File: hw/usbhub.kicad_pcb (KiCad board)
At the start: 2 copper layers, 100 x 100 mm, 92 parts, among them J1 EXT_PWR, J2 USB_C_Receptacle_USB2.0, J3 USB6, J4 USB2, J5 USB7, J6 USB3, J7 USB4, J8 USB5, J9 SWD, SW1 SW_Push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

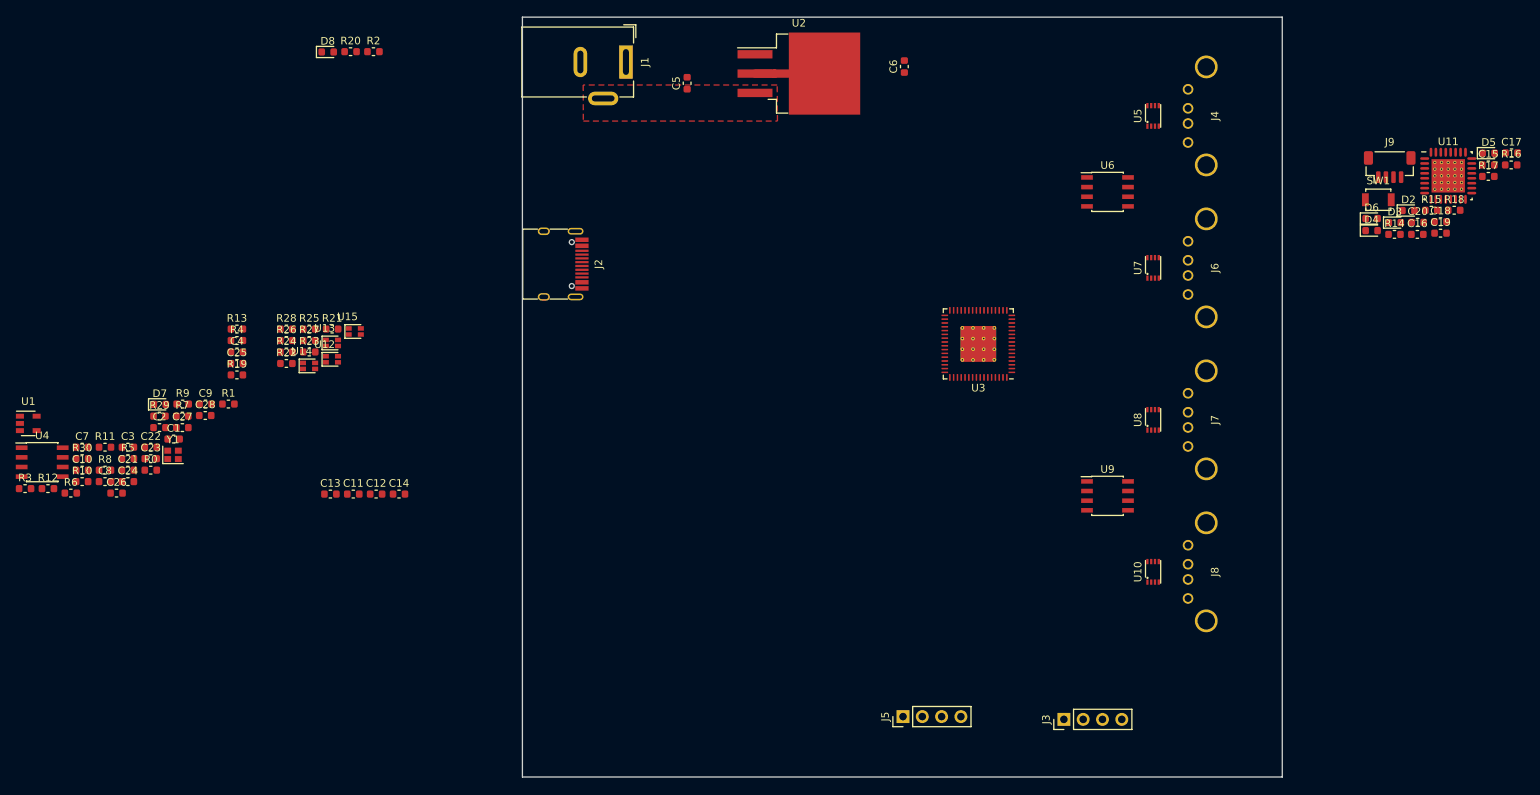
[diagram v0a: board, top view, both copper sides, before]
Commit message: More parts placement
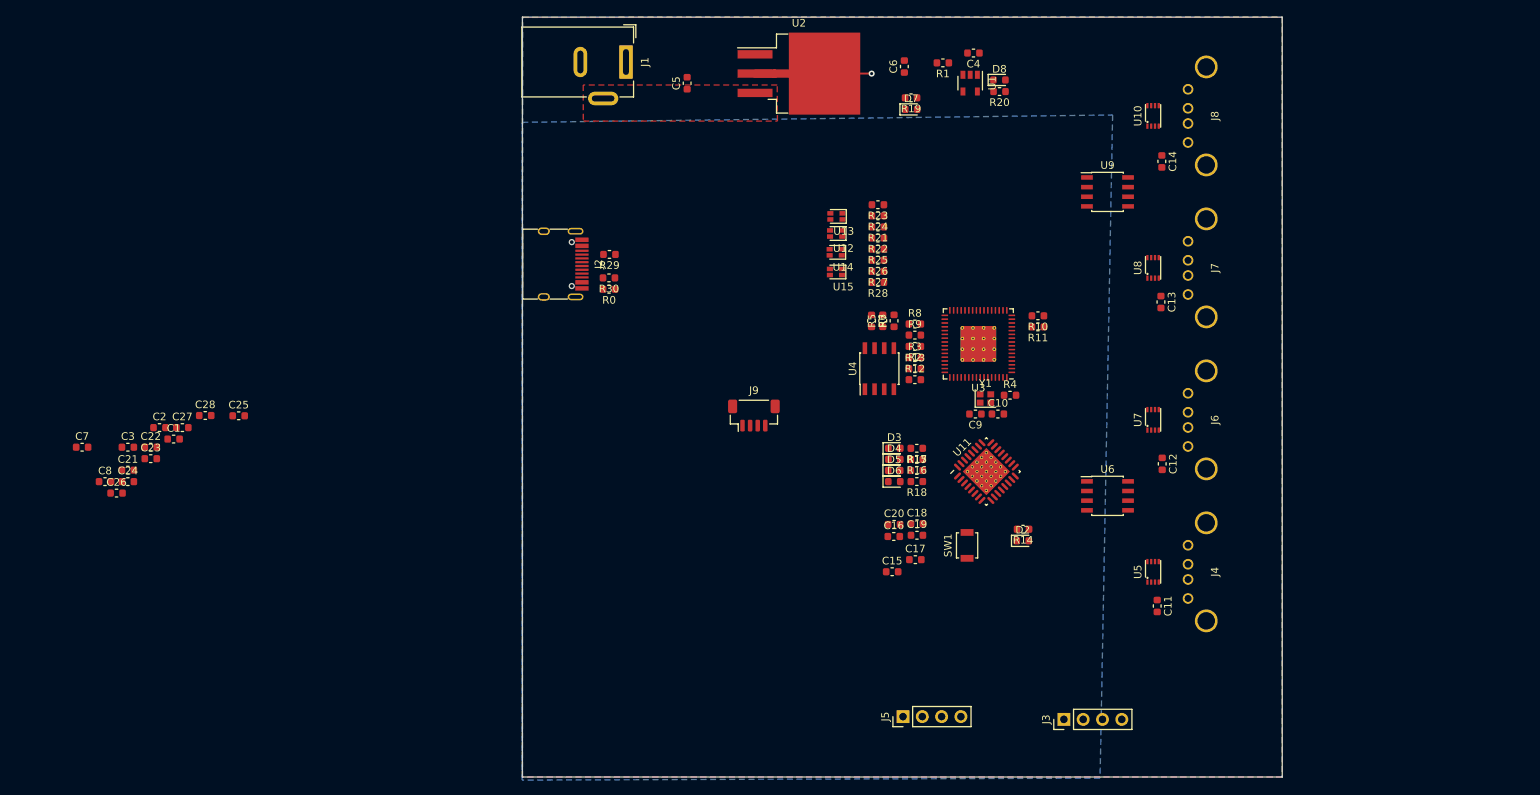
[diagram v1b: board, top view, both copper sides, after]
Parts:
- moved U1 131.8 mm to (158.9, 58.7), turned to 270 degrees
- moved R10 127.7 mm to (167.8, 89.3), turned to 180 degrees
- moved R11 123.8 mm to (167.8, 90.8), turned to 180 degrees
- moved C10 120.7 mm to (162.6, 102.2)
- moved R3 118.4 mm to (151.7, 94.8)
- moved R12 115.0 mm to (151.7, 97.7)
- moved C13 112.2 mm to (184.0, 87.5), turned to 270 degrees
- moved U4 110.9 mm to (147.0, 96.3), turned to 90 degrees
- moved C14 109.5 mm to (184.2, 69.0), turned to 270 degrees
- moved R8 108.3 mm to (151.7, 90.4)
- moved R6 107.8 mm to (145.9, 90.0), turned to 270 degrees
- moved Y1 107.2 mm to (160.9, 100.2)
- moved C11 106.8 mm to (183.5, 127.5), turned to 270 degrees
- moved D7 106.2 mm to (151.2, 62.1)
- moved C4 104.6 mm to (159.4, 54.7), turned to 180 degrees
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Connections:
- U6 pad 5: /USBPorts/USB3_VBUS -> /USBPorts/USB2_VBUS
- U6 pad 8: /USBPorts/USB2_VBUS -> /USBPorts/USB3_VBUS
- U9 pad 5: /USBPorts/USB5_VBUS -> /USBPorts/USB4_VBUS
- U9 pad 8: /USBPorts/USB4_VBUS -> /USBPorts/USB5_VBUS
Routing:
- net +5V: track 9.15 -> 15.4 mm, vias 0 -> 1
- added copper zone on B.Cu, net +5V
- added copper zone on B.Cu, net GND
- added copper zone on F.Cu, net GND

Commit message: More placement, more issues
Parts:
- removed D6: LED_Small, LED_SMD:LED_0603_1608Metric
- removed R21, R22, R23, R24, R25, R26, R27, R28: 360R, Resistor_SMD:R_0603_1608Metric
- removed U12, U13, U14, U15: LED_GRAB, LED_SMD_Extra:LED_RGB_0606_1616Metric
- added D1: G, LED_SMD:LED_0603_1608Metric, F.Cu at (194.8, 107.7)
- C11, C12, C13, C14: footprint Capacitor_SMD:C_0603_1608Metric -> Capacitor_SMD:CP_Elec_5x5.8
- D2: value Green -> VDDMCU_LED
- D3, D4, D5: value LED_Small -> G
- R0: value 0R -> DNP
- R12: value 10k -> DNP
- R15: value 360R -> 2.2k
- R16, R17, R18: value R_Small -> 2.2k
- SW1: value SW_Push -> MCU_RESET
- moved D3 66.2 mm to (194.8, 59.0), turned to 180 degrees
- moved R16 62.6 mm to (190.5, 59.0), turned to 0 degrees
- moved D5 52.9 mm to (194.8, 83.2), turned to 180 degrees
- moved D4 52.2 mm to (194.8, 133.2), turned to 180 degrees
- moved R18 47.6 mm to (190.5, 83.2)
- moved R17 45.3 mm to (190.5, 133.3), turned to 180 degrees
- moved J5 42.6 mm to (107.7, 145.2)
- moved R15 38.7 mm to (190.5, 107.7), turned to 0 degrees
- moved C15 33.3 mm to (115.5, 119.8)
- moved C16 33.3 mm to (115.7, 115.2)
- moved D2 33.3 mm to (132.7, 115.8)
- moved R14 33.3 mm to (132.7, 114.2)
- moved C18 33.3 mm to (118.8, 113.5)
- moved C19 33.3 mm to (118.8, 115.0)
- moved C20 33.3 mm to (115.8, 113.6)
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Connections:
- net /USBPorts/USB_D+ renamed /USBPorts/USB3_D+
- net Net-(C10-Pad1) renamed /USB2517/XTAL1
- net Net-(C9-Pad1) renamed /USB2517/XTAL2
- net Net-(J2-PadA5) renamed /USB2517/CC1
- net Net-(J2-PadA6) renamed /USB2517/USBUP_D+
- net Net-(J2-PadA7) renamed /USB2517/USBUP_D-
- net Net-(J2-PadB5) renamed /USB2517/CC2
- net Net-(R1-Pad1) renamed /USB2517/3V3_EN
- net Net-(R10-Pad2) renamed /USB2517/CFG_SEL2
- net Net-(R2-Pad1) renamed /USB2517/VBUS_DET
- net Net-(R4-Pad1) renamed /USB2517/RBIAS
- net Net-(R8-Pad2) renamed /USB2517/CFG_SEL1
- net Net-(SW1-Pad2) renamed /MCU/~MCU_RESET~
- R15 pad 1: /MCU/PORT2_PWR -> /USBPorts/USB3_VBUS
- R15 pad 2: Net-(D3-Pad2) -> Net-(D1-Pad2)
- R16 pad 1: /MCU/PORT3_PWR -> /USBPorts/USB5_VBUS
- R16 pad 2: Net-(D4-Pad2) -> Net-(D3-Pad2)
- R17 pad 1: /MCU/PORT4_PWR -> Net-(D4-Pad2)
- R17 pad 2: Net-(D5-Pad2) -> /USBPorts/USB2_VBUS
- R18 pad 1: /MCU/PORT5_PWR -> Net-(D5-Pad2)
- R18 pad 2: Net-(D6-Pad2) -> /USBPorts/USB4_VBUS
- U3 pad 18: /USBPorts/PORT5_LED2 -> Net-(U3-Pad18)
- U3 pad 21: Net-(U3-Pad21) -> /USBPorts/USB4_OC
- U3 pad 22: Net-(U3-Pad22) -> /USBPorts/USB3_OC
- U3 pad 27: Net-(U3-Pad27) -> /USBPorts/USB2_OC
- U3 pad 31: /USBPorts/PORT5_LED1 -> Net-(U3-Pad31)
- U3 pad 32: /USBPorts/PORT4_LED2 -> Net-(U3-Pad32)
- U3 pad 33: /USBPorts/PORT4_LED1 -> Net-(U3-Pad33)
- U3 pad 34: /USBPorts/PORT3_LED2 -> Net-(U3-Pad34)
- U3 pad 35: Net-(U3-Pad35) -> /USBPorts/USB5_OC
- U3 pad 47: /USBPorts/PORT3_LED1 -> Net-(U3-Pad47)
- U3 pad 48: /USBPorts/PORT2_LED2 -> Net-(U3-Pad48)
- U3 pad 49: /USBPorts/PORT2_LED1 -> Net-(U3-Pad49)
- U6 pad 1: /MCU/PORT2_EN -> /MCU/PORT3_EN
- U6 pad 2: Net-(U3-Pad27) -> /USBPorts/USB3_OC
- U6 pad 3: Net-(U3-Pad22) -> /USBPorts/USB2_OC
- U6 pad 4: /MCU/PORT3_EN -> /MCU/PORT2_EN
- U9 pad 1: /MCU/PORT4_EN -> /MCU/PORT5_EN
- U9 pad 2: Net-(U3-Pad21) -> /USBPorts/USB5_OC
- U9 pad 3: Net-(U3-Pad35) -> /USBPorts/USB4_OC
- U9 pad 4: /MCU/PORT5_EN -> /MCU/PORT4_EN
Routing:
- net +5V: track 15.4 -> 13.5 mm, vias 1 -> 14
- added copper zone on F.Cu, net +5V

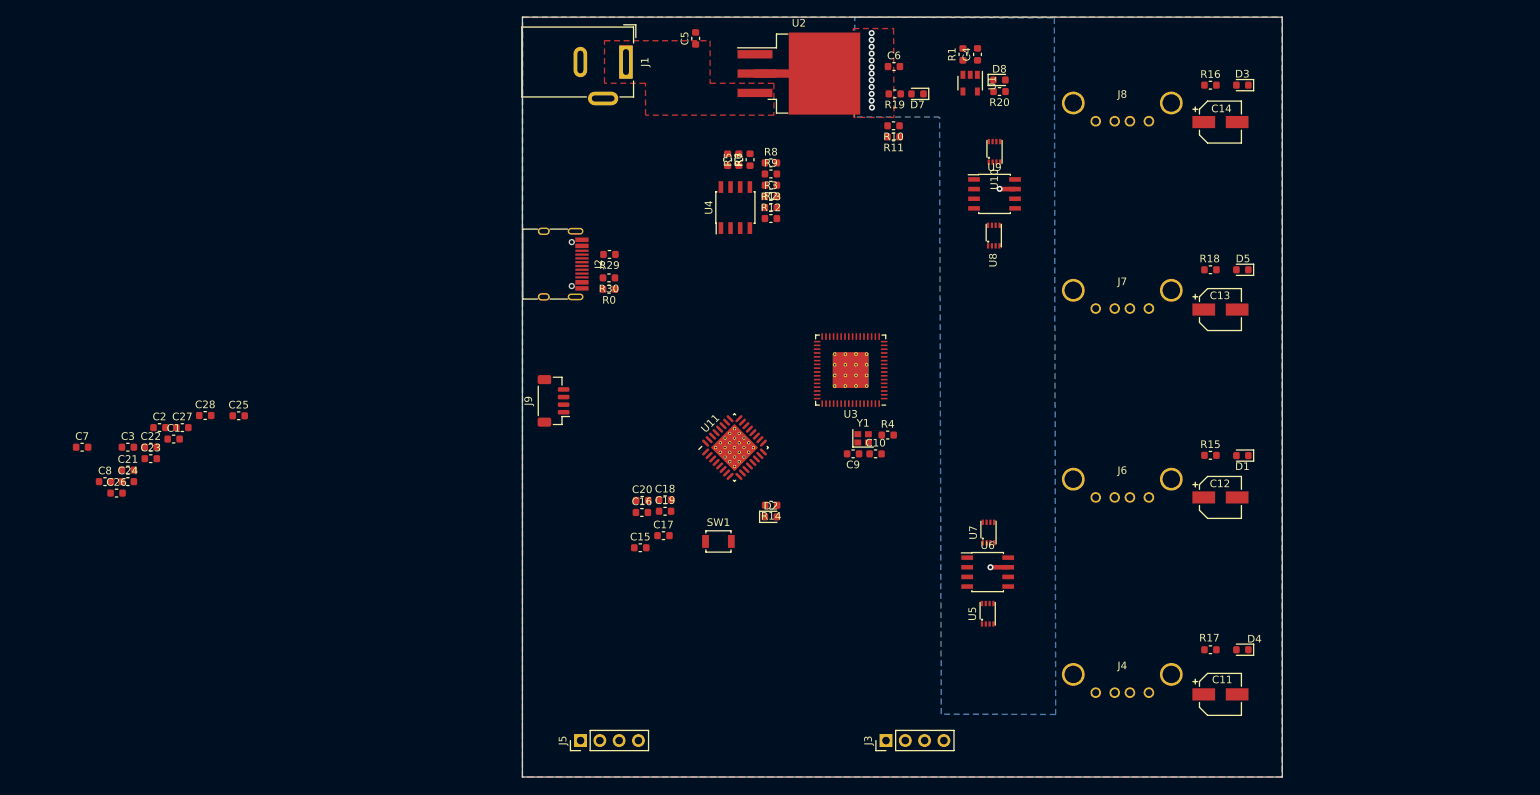
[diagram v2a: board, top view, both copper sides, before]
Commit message: More routing, simplification
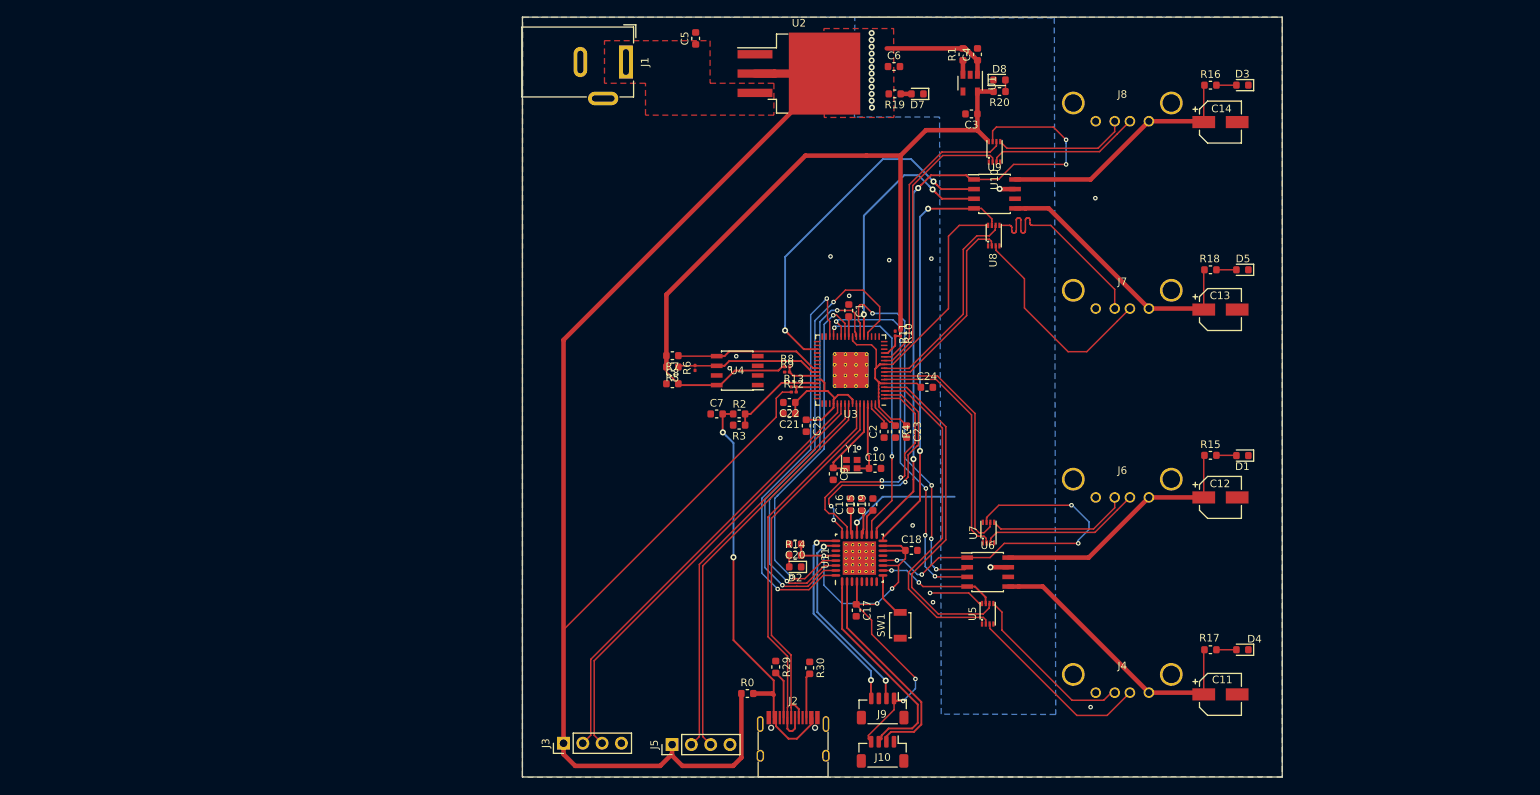
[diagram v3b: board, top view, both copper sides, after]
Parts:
- removed C26, C27, C28: 0.1uF, Capacitor_SMD:C_0603_1608Metric
- added J10: DBG_UART, Connector_JST:JST_SH_BM04B-SRSS-TB_1x04-1MP_P1.00mm_Vertical, F.Cu at (147.4, 146.7)
- R10, R11, R12, R13, R6, R8, R9: footprint Resistor_SMD:R_0603_1608Metric -> Resistor_SMD:R_0201_0603Metric
- moved C3 119.4 mm to (159.1, 62.7), turned to 180 degrees
- moved C24 105.9 mm to (153.2, 98.7)
- moved C23 99.5 mm to (150.6, 104.5), turned to 270 degrees
- moved C2 95.4 mm to (147.6, 104.5), turned to 90 degrees
- moved C1 90.4 mm to (143.0, 88.6), turned to 270 degrees
- moved C21 87.4 mm to (135.1, 102.2), turned to 180 degrees
- moved C22 84.2 mm to (135.1, 100.7), turned to 180 degrees
- moved C7 83.6 mm to (125.6, 102.2)
- moved C8 75.8 mm to (119.7, 98.2)
- moved C25 74.7 mm to (137.4, 103.8), turned to 270 degrees
- moved J2 70.0 mm to (135.6, 145.3), turned to 0 degrees
- moved J9 59.3 mm to (147.4, 141.0), turned to 180 degrees
- moved R29 58.5 mm to (133.3, 135.5), turned to 270 degrees
- moved R30 57.7 mm to (137.8, 135.6), turned to 270 degrees
- moved R0 56.2 mm to (129.6, 139.0), turned to 0 degrees
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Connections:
- net Net-(C1-Pad2) renamed /USB2517/VDD18
- net Net-(C2-Pad2) renamed /USB2517/VDD18PLL
- U11 pad 1: /MCU/PORT2_PWR -> Net-(J10-Pad3)
- U11 pad 13: /MCU/PORT4_EN -> Net-(U11-Pad13)
- U11 pad 16: /MCU/PORT5_EN -> /MCU/PORT4_EN
- U11 pad 17: Net-(U11-Pad17) -> /MCU/PORT5_EN
- U11 pad 2: /MCU/PORT3_PWR -> Net-(J10-Pad2)
- U11 pad 29: Net-(U11-Pad29) -> /MCU/PORT2_PWR
- U11 pad 30: Net-(U11-Pad30) -> /MCU/PORT3_PWR
- U11 pad 31: Net-(U11-Pad31) -> /MCU/PORT4_PWR
- U11 pad 32: Net-(U11-Pad32) -> /MCU/PORT5_PWR
- U11 pad 5: /MCU/PORT4_PWR -> Net-(U11-Pad5)
- U11 pad 6: /MCU/PORT5_PWR -> Net-(U11-Pad6)
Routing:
- net +5V: track 13.5 -> 227.5 mm, vias 14 -> 15
- net +3V3: track 0.00 -> 186.2 mm, vias 0 -> 1
- net /MCU/PORT5_EN: track 0.00 -> 84.3 mm, vias 0 -> 4
- net VDDMCU: track 0.00 -> 72.7 mm, vias 0 -> 5
- net /MCU/PORT4_PWR: track 0.00 -> 62.1 mm, vias 0 -> 2
- net /USBPorts/PORT6_D-: track 0.00 -> 58.6 mm
- net /USBPorts/PORT6_D+: track 0.00 -> 58.6 mm
- net /MCU/PORT5_PWR: track 0.00 -> 56.3 mm, vias 0 -> 2
- net /MCU/PORT4_EN: track 0.00 -> 56.0 mm, vias 0 -> 2
- net VBUS: track 0.00 -> 55.1 mm, vias 0 -> 2
- net /MCU/PORT3_PWR: track 0.00 -> 53.9 mm, vias 0 -> 2
- net /USBPorts/PORT7_D-: track 0.00 -> 53.3 mm
- net /USBPorts/PORT7_D+: track 0.00 -> 53.3 mm
- net /USB2517/USBUP_D-: track 0.00 -> 51.4 mm
- net /USBPorts/USB2_OC: track 0.00 -> 50.2 mm, vias 0 -> 4
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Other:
- rule via_min_size: 0.4 -> 0.6

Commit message: Final
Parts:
- added REF**: OSHW-Symbol_13.4x12mm_SilkScreen, Symbol:OSHW-Symbol_13.4x12mm_SilkScreen, F.Cu at (123.7, 79.9)
- added REF**: KiCad-Logo_6mm_SilkScreen, Symbol:KiCad-Logo_6mm_SilkScreen, F.Cu at (187.3, 145.2)
- added REF**: Polarity_Center_Positive_6mm_SilkScreen, Symbol:Polarity_Center_Positive_6mm_SilkScreen, B.Cu at (113.7, 68.6)
- added TP1: EEPROM_SDA, TestPoint:TestPoint_Pad_D1.0mm, F.Cu at (134.8, 93.9)
- added TP10: OCS5_N, TestPoint:TestPoint_Pad_D1.0mm, F.Cu at (155.6, 72.5)
- added TP11: USB_MCU_D-, TestPoint:TestPoint_Pad_D1.0mm, F.Cu at (139.6, 115.4)
- added TP12: USB_MCU_D+, TestPoint:TestPoint_Pad_D1.0mm, F.Cu at (141.4, 113.3)
- added TP13: VBUS_DETECT, TestPoint:TestPoint_Pad_D1.0mm, F.Cu at (148.7, 112.7)
- added TP14: PORT2_EN, TestPoint:TestPoint_Pad_D1.0mm, F.Cu at (153.4, 124.4)
- added TP15: PORT3_EN, TestPoint:TestPoint_Pad_D1.0mm, F.Cu at (168.2, 119.3)
- added TP16: PORT4_EN, TestPoint:TestPoint_Pad_D1.0mm, F.Cu at (155.1, 75.2)
- added TP17: PORT5_EN, TestPoint:TestPoint_Pad_D1.0mm, F.Cu at (167.9, 69.4)
- added TP18: PORT2_PWR, TestPoint:TestPoint_Pad_D1.0mm, F.Cu at (137.6, 123.9)
- added TP19: PORT3_PWR, TestPoint:TestPoint_Pad_D1.0mm, F.Cu at (135.8, 124.9)
- added TP2: EEPROM_SCL, TestPoint:TestPoint_Pad_D1.0mm, F.Cu at (133.1, 95.3)
- added TP20: PORT4_PWR, TestPoint:TestPoint_Pad_D1.0mm, F.Cu at (137.5, 126.1)
- added TP21: PORT5_PWR, TestPoint:TestPoint_Pad_D1.0mm, F.Cu at (135.4, 127.3)
- added TP4: VBUS_DET, TestPoint:TestPoint_Pad_D1.0mm, F.Cu at (130.2, 100.3)
- added TP5: USB_UP_D-, TestPoint:TestPoint_Pad_D1.0mm, F.Cu at (131.8, 129.4)
- added TP6: USBUP_D+, TestPoint:TestPoint_Pad_D1.0mm, F.Cu at (132.8, 127.6)
- added TP7: OSC2_N, TestPoint:TestPoint_Pad_D1.0mm, F.Cu at (156.3, 123.6)
- added TP8: OCS3_N, TestPoint:TestPoint_Pad_D1.0mm, F.Cu at (154.8, 122.4)
- added TP9: OCS4_N, TestPoint:TestPoint_Pad_D1.0mm, F.Cu at (157.2, 73.9)
- C8: value 0.1uF -> DNP
- J10, J9: footprint Connector_JST:JST_SH_BM04B-SRSS-TB_1x04-1MP_P1.00mm_Vertical -> Connector_PinHeader_2.54mm:PinHeader_1x04_P2.54mm_Vertical
- R5, R7: value 10k -> DNP
- R6: value DNP -> 10k; footprint Resistor_SMD:R_0201_0603Metric -> Resistor_SMD:R_0603_1608Metric
- SW1: footprint Button_Switch_SMD:SW_SPST_B3U-1000P -> Button_Switch_SMD:SW_SPST_FSMSM
- U4: value 24LC02 -> DNP/24LC02
- moved J10 17.1 mm to (164.5, 145.6), turned to 270 degrees
- moved SW1 12.4 mm to (159.9, 137.2), turned to 180 degrees
- moved J9 6.06 mm to (151.4, 145.6), turned to 270 degrees
- moved C1 0.52 mm to (142.7, 88.2)
- moved R6 0.51 mm to (122.9, 96.6)
- moved R30 0.46 mm to (137.4, 135.6)
- moved J5 0.18 mm to (119.7, 145.6)
- moved R8 0.13 mm to (134.9, 95.9)
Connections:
- net Net-(J10-Pad2) renamed /MCU/UART_TX
- net Net-(J10-Pad3) renamed /MCU/UART_RX
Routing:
- net +3V3: track 186.2 -> 299.3 mm, vias 1 -> 14
- net VDDMCU: track 72.7 -> 86.5 mm, vias 5 -> 6
- net /MCU/~MCU_RESET~: track 6.04 -> 18.4 mm
- net /MCU/MCU_SWDCLK: track 26.4 -> 33.2 mm
- net /MCU/MCU_SWDIO: track 25.7 -> 32.0 mm
- net GND: track 0.00 -> 4.75 mm, vias 13 -> 24
- net /MCU/PORT5_PWR: track 56.3 -> 59.8 mm
- net /MCU/UART_TX: track 28.8 -> 31.6 mm
- net /MCU/PORT3_PWR: track 53.9 -> 55.7 mm
- net +5V: track 227.5 -> 229.2 mm, vias 15 -> 21
- net /MCU/PORT4_PWR: track 62.1 -> 63.3 mm
- net /MCU/USB_MCU_D-: track 32.1 -> 33.0 mm
- net /USB2517/VBUS_DET: track 12.7 -> 13.5 mm
- net /USBPorts/USB3_OC: track 49.8 -> 48.9 mm
- net /MCU/USB_MCU_D+: track 32.1 -> 31.2 mm
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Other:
- outline, holes or cut-outs redrawn
- board text added: "+3v3"
- board text added: "+5V"
- board text added: "7-16V"
- board text added: "D+"
- board text added: "D-"
- board text added: "GND"
- board text added: "RESET"
- board text added: "RX"
- board text added: "SWD"
- board text added: "SWDCLK"
- board text added: "SWDIO"
- board text added: "Smart USB HUB Rev 0.1 20181205"
- board text added: "TX"
- board text added: "UART"
- board text added: "USB2"
- board text added: "USB3"
- board text added: "USB4"
- board text added: "USB5"
- board text added: "USB6"
- board text added: "USB7"
- board text added: "https://github.com/EnJens/smarthub"
